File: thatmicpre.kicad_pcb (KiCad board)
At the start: 2 copper layers, 45 x 24 mm, 12 parts, among them J1 Conn_01x07_Female, U1 THAT1512

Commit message: rev3 board: place and route R3-R6, C7, C8; sync nets and part data
Same outline, J1 position and pinout, and M3 hole: a drop-in for rev2.
- R4/C7 (+15V filter) in the free pocket beside J1; R6 (gain stop) on the
  RV1-C6 track along the top edge; R3 (output build-out), R5/C8 (-15V
  filter) between U1, C6 and H4. Out now leaves U1 through R3.
- -15V_F returns to C4/U1 pin 4 on a short B.Cu run; C4's ground gets a
  direct F.Cu track to U1 pin 5, and C4 pad 1 / J1 pad 3 connect solid to
  the pour (both were starved thermals; J1's dates from rev2).
- Nets, values and Vendor fields synced to the rev3 schematic; footprint
  paths point at the schematic symbols. Removed a stray 1.3 mm cross on
  the Margin layer under U1 that DRC treats as board edge.
- Silk: "THAT1512 rev3" on the front, name/rev on the back; new parts
  show values only, as rev2 does. Title block rev 3.
- 3D models moved to KiCad 10's .step library; RV1 gets the square 3362P
  model from 3dmodels/ instead of the round 3339P.

Headless pcbnew (bundled interpreter), one footprint load per process.
kicad-cli DRC with schematic parity: 0 errors, 0 unconnected, 0 parity.
Remaining warnings predate rev3 (KiCad 6 footprint copies, 0.7 mm silk
text, the Trimmer library path, the JLC order-number placeholder).

Co-Authored-By: Claude Opus 5.5 <noreply@anthropic.com>
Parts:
- added C7: 10u, Capacitor_THT:CP_Radial_D5.0mm_P2.00mm, F.Cu at (93.4, 56.0)
- added C8: 10u, Capacitor_THT:CP_Radial_D5.0mm_P2.00mm, F.Cu at (119.1, 69.0)
- added R3: 100R, Resistor_THT:R_Axial_DIN0204_L3.6mm_D1.6mm_P2.54mm_Vertical, F.Cu at (115.0, 67.6)
- added R4: 10R, Resistor_THT:R_Axial_DIN0204_L3.6mm_D1.6mm_P2.54mm_Vertical, F.Cu at (91.3, 60.6)
- added R5: 10R, Resistor_THT:R_Axial_DIN0204_L3.6mm_D1.6mm_P2.54mm_Vertical, F.Cu at (116.6, 74.9)
- added R6: 5R6, Resistor_THT:R_Axial_DIN0207_L6.3mm_D2.5mm_P2.54mm_Vertical, F.Cu at (107.5, 55.1)
- C6: value 6800μ -> 6800u
- J1: value Conn_01x07_Female -> PinHeader_1x07
- U1: value THAT1512 -> THAT1512P08-U
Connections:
- C4 pad 2: -15V -> /-15V_F
- C5 pad 2: +15V -> /+15V_F
- C6 pad 1: Net-(RV1-Pad3) -> Net-(C6-Pad1)
- RV1 pad 3: Net-(RV1-Pad3) -> Net-(R6-Pad1)
- U1 pad 4: -15V -> /-15V_F
- U1 pad 6: Out -> Net-(R3-Pad1)
- U1 pad 7: +15V -> /+15V_F
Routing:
- net /+15V_F: track 0.00 -> 27.8 mm
- net Net-(RV1-Pad3): track 27.7 -> 0.00 mm
- net +15V: track 31.9 -> 4.88 mm
- net /-15V_F: track 0.00 -> 22.3 mm
- net Net-(C6-Pad1): track 0.00 -> 17.1 mm
- net Net-(R6-Pad1): track 0.00 -> 8.11 mm
- net GND: track 0.00 -> 4.44 mm
- net -15V: track 39.3 -> 42.1 mm
- net Net-(R3-Pad1): track 0.00 -> 2.72 mm
- net Out: track 52.4 -> 53.2 mm
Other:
- board text added: "THAT1512 Mic Pre rev3 2026"
- board text added: "THAT1512 rev3"
- board text removed: "2022 rev2"
- board text removed: "THAT1512 Mic Pre"

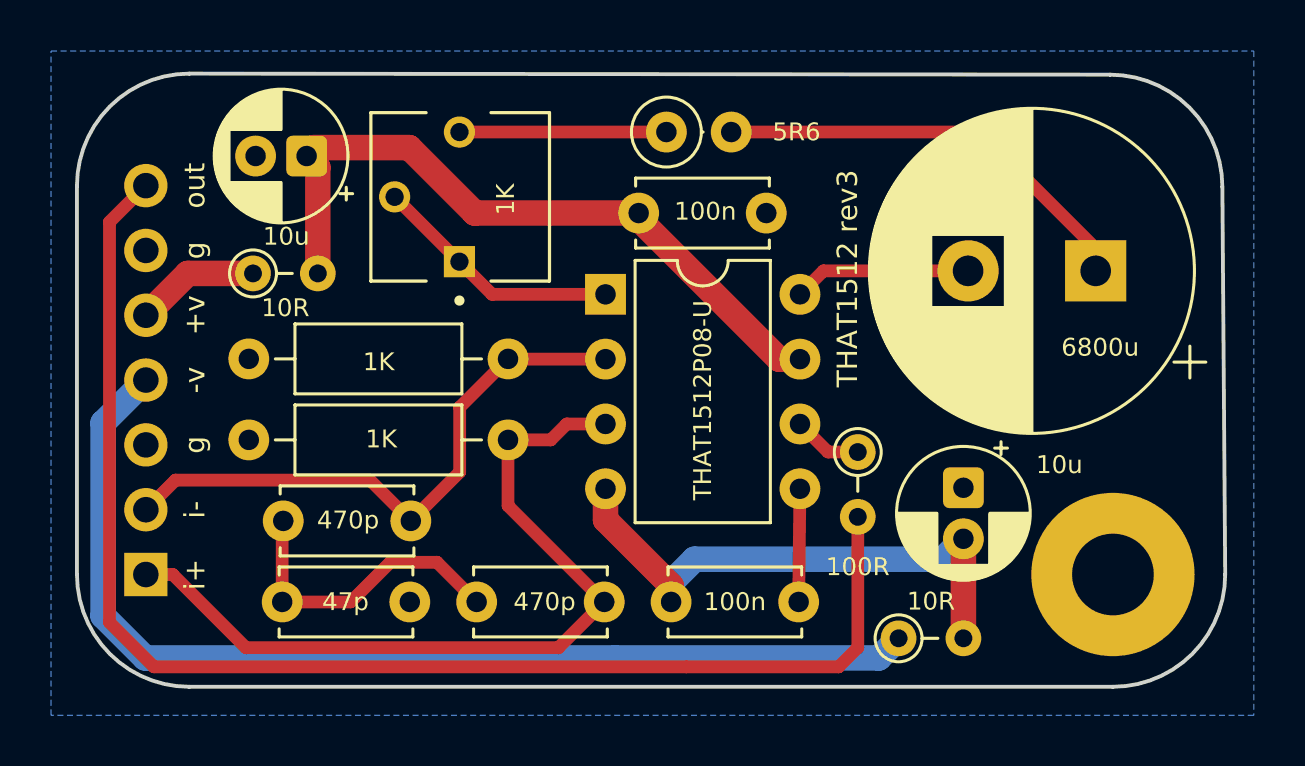
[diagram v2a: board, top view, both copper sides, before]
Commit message: rev3: rounded tracks, README, schematic PDF, render
- Tracks filleted in the board itself (40 corners, radius up to 2 mm) with
  the tooling lane's fillet_adaptive.py run headless, instead of rev2's
  separate -rounded copy; unfillet() in that script restores the corners.
  DRC with schematic parity unchanged: 0 errors, 0 unconnected, 0 parity.
- README: rev3 changes, gain range, BOM with the corrected part numbers.
  C6's part number is left blank: the fitted part is not recorded.
- schematic.pdf regenerated from the rev3 schematic; kicad-cli render.

Co-Authored-By: Claude Opus 5.5 <noreply@anthropic.com>
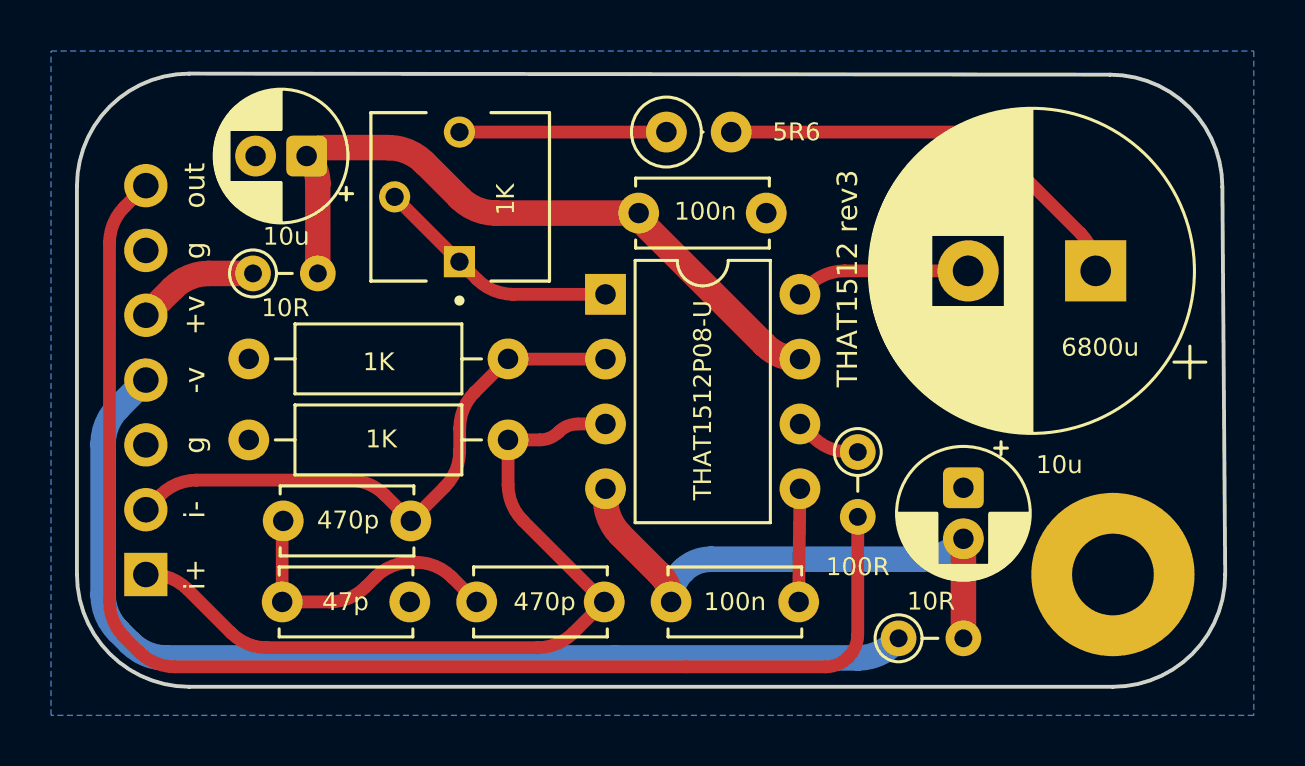
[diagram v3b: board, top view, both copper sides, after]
